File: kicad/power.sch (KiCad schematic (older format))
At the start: 18 parts

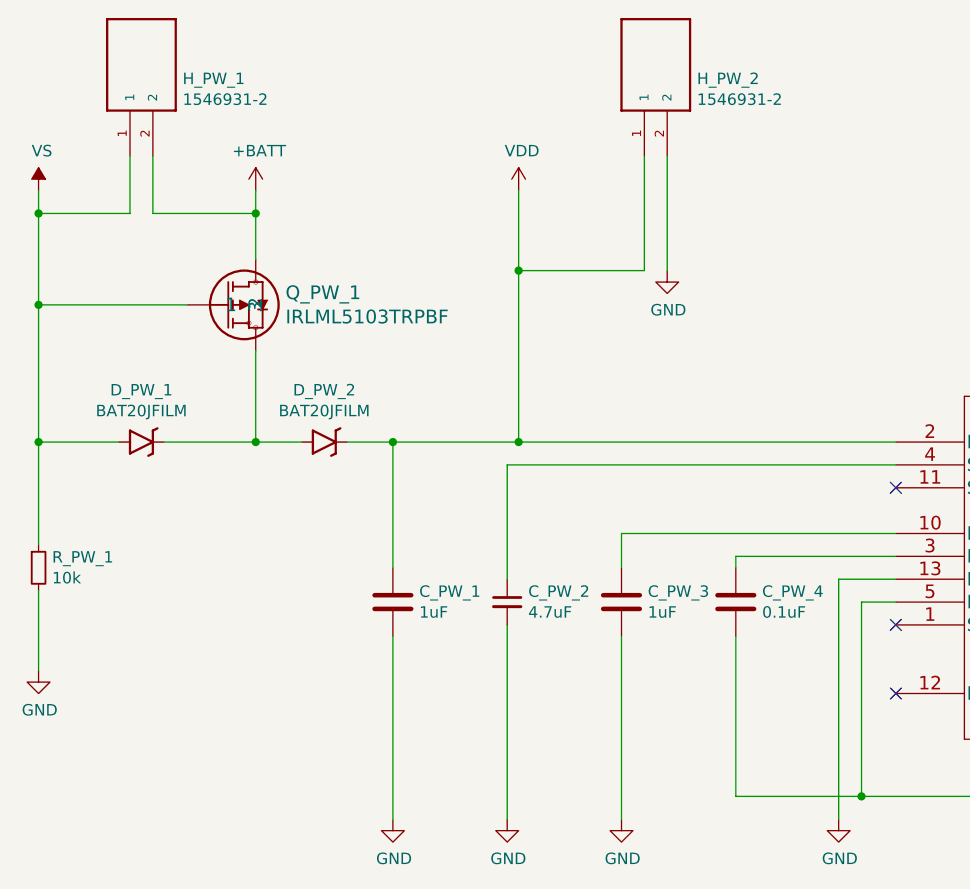
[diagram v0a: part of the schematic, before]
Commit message: Deleted a header pin. Started working on PCB
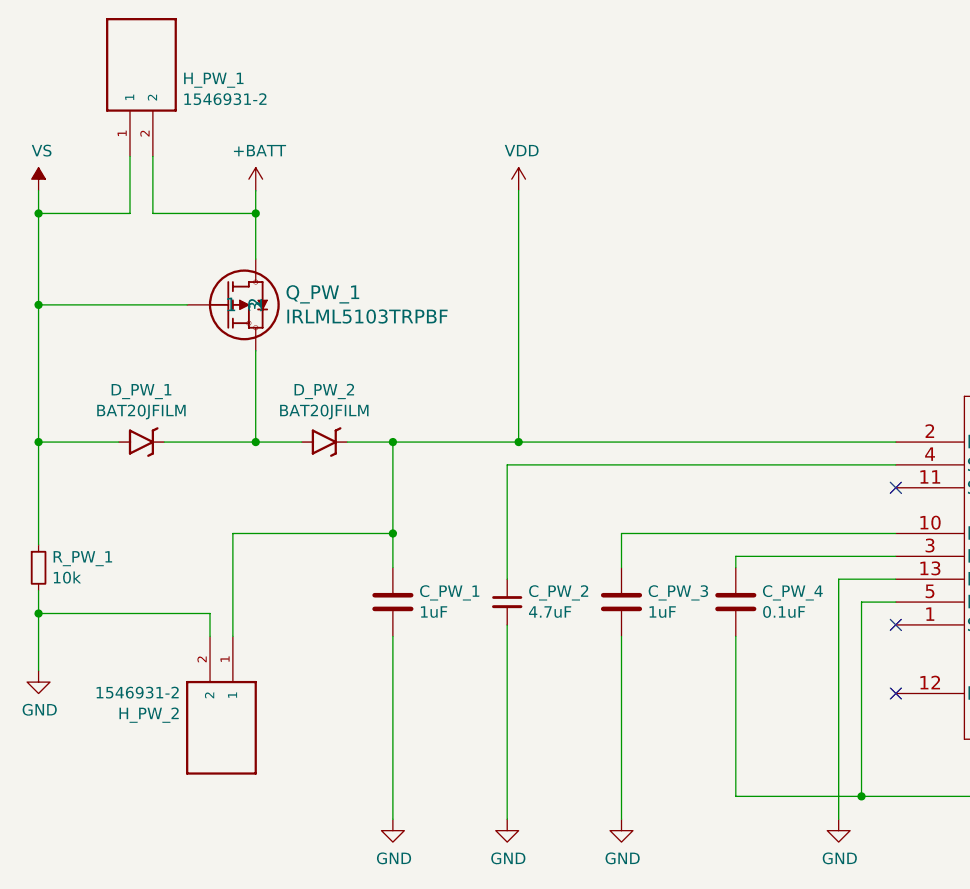
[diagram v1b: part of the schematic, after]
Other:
- moved on the sheet: H_PW_2
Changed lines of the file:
@@
 $Descr A4 11693 8268
 encoding utf-8
-Sheet 2 6
+Sheet 2 5
 Title "ESP32 Sensor Module | Power Supply"
 Date "2020-11-23"
@@
 $EndComp
 $Comp
-L power:+BATT #PWR?
+L power:+BATT #PWR0101
 U 1 1 5FB6F3E3
 P 1850 2200
-F 0 "#PWR?" H 1850 2050 50  0001 C CNN
+F 0 "#PWR0101" H 1850 2050 50  0001 C CNN
 F 1 "+BATT" H 1865 2373 50  0000 C CNN
 F 2 "" H 1850 2200 50  0001 C CNN
@@
 $EndComp
 $Comp
-L power:GND #PWR?
+L power:GND #PWR0102
 U 1 1 5FB9CCF4
 P 3450 4950
-F 0 "#PWR?" H 3450 4700 50  0001 C CNN
+F 0 "#PWR0102" H 3450 4700 50  0001 C CNN
 F 1 "GND" H 3455 4777 50  0000 C CNN
 F 2 "" H 3450 4950 50  0001 C CNN
@@
 $EndComp
 $Comp
-L power:GND #PWR?
+L power:GND #PWR0103
 U 1 1 5FB9D2E5
 P 2950 4950
-F 0 "#PWR?" H 2950 4700 50  0001 C CNN
+F 0 "#PWR0103" H 2950 4700 50  0001 C CNN
 F 1 "GND" H 2955 4777 50  0000 C CNN
 F 2 "" H 2950 4950 50  0001 C CNN
@@
 $EndComp
 $Comp
-L power:GND #PWR?
+L power:GND #PWR0104
 U 1 1 5FC8EA7A
 P 2450 4950
-F 0 "#PWR?" H 2450 4700 50  0001 C CNN
+F 0 "#PWR0104" H 2450 4700 50  0001 C CNN
 F 1 "GND" H 2455 4777 50  0000 C CNN
 F 2 "" H 2450 4950 50  0001 C CNN
@@
 	2450 4150 2450 4950
 $Comp
-L power:VDD #PWR?
+L power:VDD #PWR0105
 U 1 1 5FC9DE63
 P 3000 2200
-F 0 "#PWR?" H 3000 2050 50  0001 C CNN
+F 0 "#PWR0105" H 3000 2050 50  0001 C CNN
 F 1 "VDD" H 3015 2373 50  0000 C CNN
 F 2 "" H 3000 2200 50  0001 C CNN
@@
 $EndComp
 $Comp
-L power:GND #PWR?
+L power:GND #PWR0106
 U 1 1 5FCA653B
 P 900 4300
-F 0 "#PWR?" H 900 4050 50  0001 C CNN
+F 0 "#PWR0106" H 900 4050 50  0001 C CNN
 F 1 "GND" H 905 4127 50  0000 C CNN
 F 2 "" H 900 4300 50  0001 C CNN
@@
 $EndComp
 Wire Wire Line
-	900  4300 900  3950
+	900  4300 900  4050
 Wire Wire Line
 	900  3750 900  3300
@@
 $EndComp
 $Comp
-L power:+3.3V #PWR?
+L power:+3.3V #PWR0107
 U 1 1 5FBC3E26
 P 9200 2800
-F 0 "#PWR?" H 9200 2650 50  0001 C CNN
+F 0 "#PWR0107" H 9200 2650 50  0001 C CNN
 F 1 "+3.3V" H 9215 2973 50  0000 C CNN
 F 2 "" H 9200 2800 50  0001 C CNN
@@
 	9200 4950 9200 4150
 $Comp
-L power:GND #PWR?
+L power:GND #PWR0108
 U 1 1 5FBC26F8
 P 9200 4950
-F 0 "#PWR?" H 9200 4700 50  0001 C CNN
+F 0 "#PWR0108" H 9200 4700 50  0001 C CNN
 F 1 "GND" H 9205 4777 50  0000 C CNN
 F 2 "" H 9200 4950 50  0001 C CNN
@@
 	7250 4950 7250 4500
 $Comp
-L power:GND #PWR?
+L power:GND #PWR0109
 U 1 1 5FBBD9E3
 P 7250 4950
-F 0 "#PWR?" H 7250 4700 50  0001 C CNN
+F 0 "#PWR0109" H 7250 4700 50  0001 C CNN
 F 1 "GND" H 7255 4777 50  0000 C CNN
 F 2 "" H 7250 4950 50  0001 C CNN
@@
 	4650 3900 4400 3900
 $Comp
-L power:GND #PWR?
+L power:GND #PWR0110
 U 1 1 5FB9D73C
 P 4400 4950
-F 0 "#PWR?" H 4400 4700 50  0001 C CNN
+F 0 "#PWR0110" H 4400 4700 50  0001 C CNN
 F 1 "GND" H 4405 4777 50  0000 C CNN
 F 2 "" H 4400 4950 50  0001 C CNN
@@
 	6250 3900 6500 3900
 $Comp
-L power:GND #PWR?
+L power:GND #PWR0111
 U 1 1 5FB7470B
 P 6500 4000
-F 0 "#PWR?" H 6500 3750 50  0001 C CNN
+F 0 "#PWR0111" H 6500 3750 50  0001 C CNN
 F 1 "GND" H 6505 3827 50  0000 C CNN
 F 2 "" H 6500 4000 50  0001 C CNN
@@
 	2250 3300 2450 3300
 Wire Wire Line
-	2450 3850 2450 3300
+	2450 3850 2450 3700
 Connection ~ 2450 3300
 Wire Wire Line
 	2450 3300 3000 3300
 $Comp
-L power:VS #PWR?
+L power:VS #PWR0112
 U 1 1 5FDE6D6A
 P 900 2200
-F 0 "#PWR?" H 700 2050 50  0001 C CNN
+F 0 "#PWR0112" H 700 2050 50  0001 C CNN
 F 1 "VS" H 915 2373 50  0000 C CNN
 F 2 "" H 900 2200 50  0001 C CNN
@@
 L 1546931-2:1546931-2 H_PW_2
 U 1 1 5FDE97E8
-P 3650 1650
-F 0 "H_PW_2" V 3589 1520 50  0000 R CNN
-F 1 "1546931-2" V 3498 1520 50  0000 R CNN
-F 2 "footprints:1546931-2" H 3650 1650 50  0001 L BNN
-F 3 "https://www.te.com/commerce/DocumentDelivery/DDEController?Action=srchrtrv&DocNm=1-1773458-1_EURO_STYLE_QRG&DocType=DS&DocLang=English" H 3650 1650 50  0001 L BNN
-F 4 "1546931-2" H 3650 1650 50  0001 C CNN "Part Name"
-F 5 "TE Connectivity AMP Connectors" H 3650 1650 50  0001 C CNN "Manufacturer"
-F 6 "Digikey Canada" H 3650 1650 50  0001 C CNN "Vendor"
-F 7 "" H 3650 1650 50  0001 C CNN "digikeypn"
-F 8 "" H 3650 1650 50  0001 C CNN "Vendor Part Number"
-F 9 "A97965-ND" H 3650 1650 50  0001 C CNN "Vendor Part Name"
-	1    3650 1650
-	0    -1   -1   0
-$EndComp
-Wire Wire Line
-	3000 2200 3000 2550
-Wire Wire Line
-	3550 2050 3550 2550
-Wire Wire Line
-	3550 2550 3000 2550
-Connection ~ 3000 2550
-Wire Wire Line
-	3000 2550 3000 3300
-$Comp
-L power:GND #PWR?
-U 1 1 5FDF0ABA
-P 3650 2550
-F 0 "#PWR?" H 3650 2300 50  0001 C CNN
-F 1 "GND" H 3655 2377 50  0000 C CNN
-F 2 "" H 3650 2550 50  0001 C CNN
-F 3 "" H 3650 2550 50  0001 C CNN
-	1    3650 2550
-	1    0    0    -1
-$EndComp
-Wire Wire Line
-	3650 2550 3650 2050
+P 1650 4550
+F 0 "H_PW_2" V 1589 4420 50  0000 R CNN
+F 1 "1546931-2" V 1498 4420 50  0000 R CNN
+F 2 "footprints:1546931-2" H 1650 4550 50  0001 L BNN
+F 3 "https://www.te.com/commerce/DocumentDelivery/DDEController?Action=srchrtrv&DocNm=1-1773458-1_EURO_STYLE_QRG&DocType=DS&DocLang=English" H 1650 4550 50  0001 L BNN
+F 4 "1546931-2" H 1650 4550 50  0001 C CNN "Part Name"
+F 5 "TE Connectivity AMP Connectors" H 1650 4550 50  0001 C CNN "Manufacturer"
+F 6 "Digikey Canada" H 1650 4550 50  0001 C CNN "Vendor"
+F 7 "" H 1650 4550 50  0001 C CNN "digikeypn"
+F 8 "" H 1650 4550 50  0001 C CNN "Vendor Part Number"
+F 9 "A97965-ND" H 1650 4550 50  0001 C CNN "Vendor Part Name"
+	1    1650 4550
+	0    1    1    0
+$EndComp
+Wire Wire Line
+	3000 2200 3000 3300
+Wire Wire Line
+	1650 4150 1650 4050
+Wire Wire Line
+	1650 4050 900  4050
+Connection ~ 900  4050
+Wire Wire Line
+	900  4050 900  3950
+Wire Wire Line
+	1750 4150 1750 3700
+Wire Wire Line
+	1750 3700 2450 3700
+Connection ~ 2450 3700
+Wire Wire Line
+	2450 3700 2450 3300
 $EndSCHEMATC

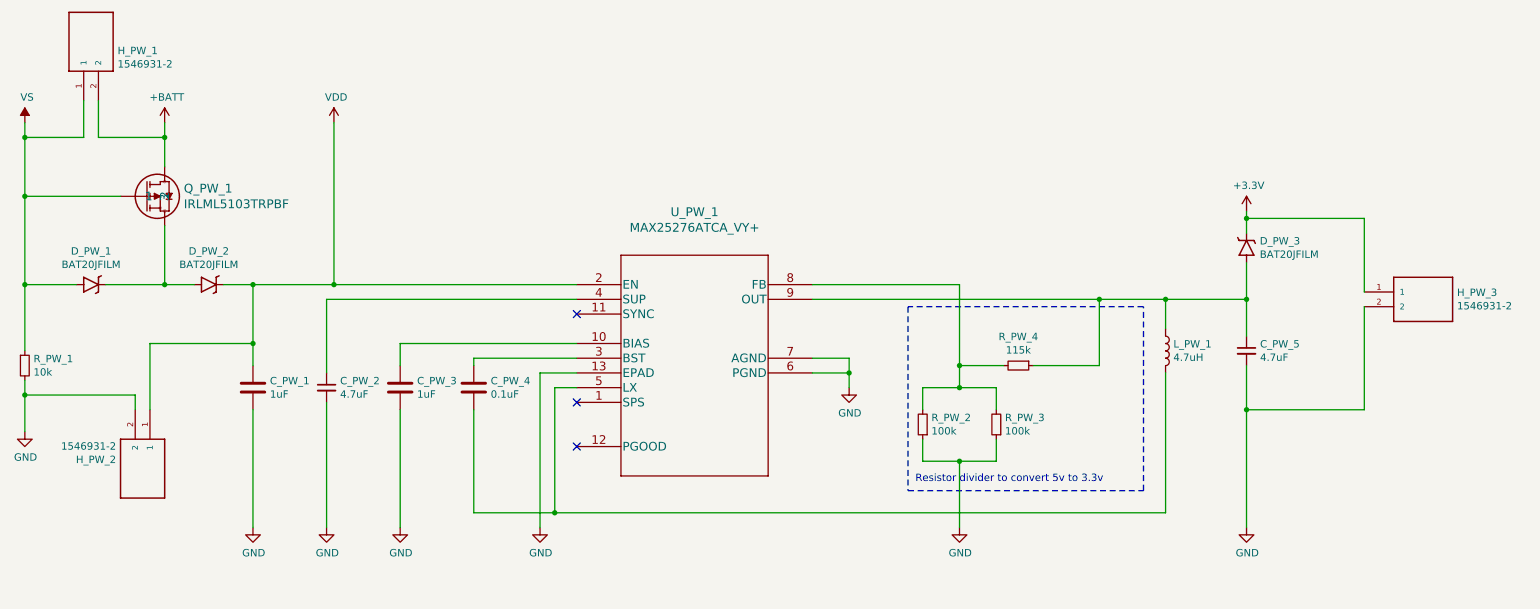
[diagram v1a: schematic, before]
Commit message: Updated schematic and PCB design to v0.0.2 for 2-layer pcb. Added more silkscreen text
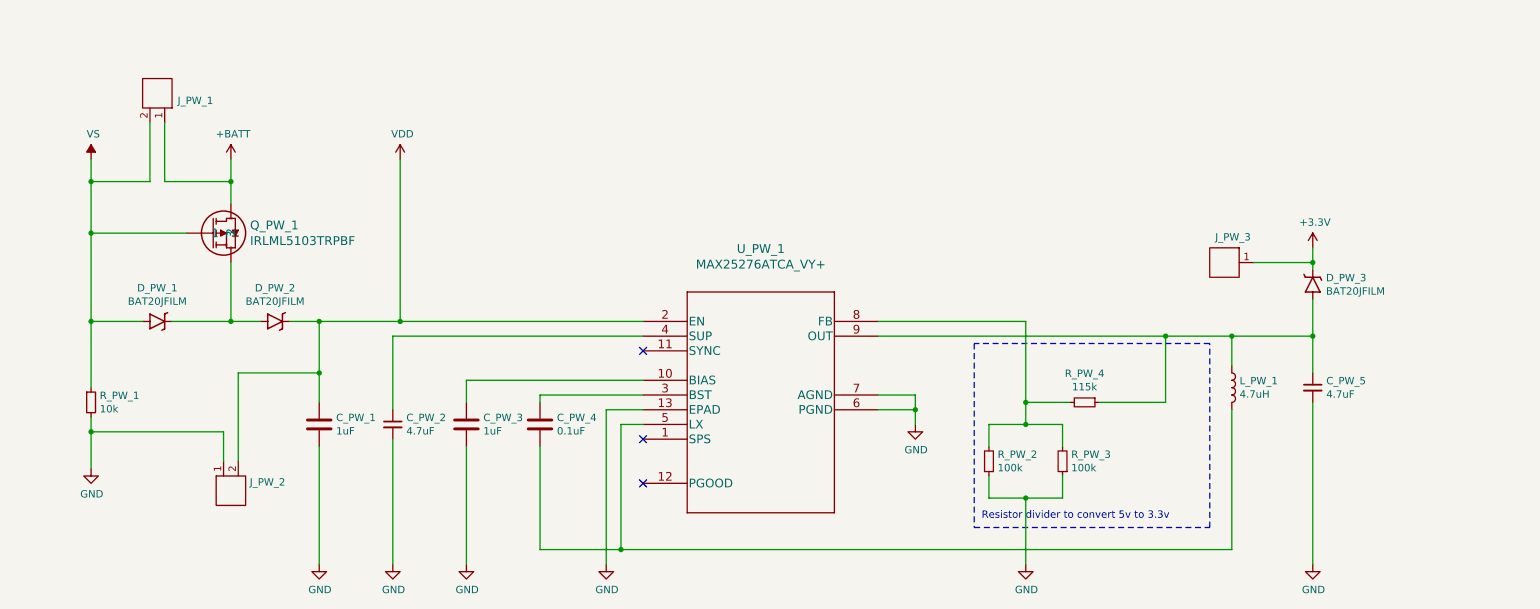
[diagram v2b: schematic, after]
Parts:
- removed H_PW_1, H_PW_2, H_PW_3: 1546931-2, footprints:1546931-2, symbol 1546931-2:1546931-2
- added J_PW_1, J_PW_2: Header_Pin_2, Connector_PinHeader_2.54mm:PinHeader_1x02_P2.54mm_Vertical, symbol CANtech:Header_Pin_2
- added J_PW_3: Header_Pin_1, Connector_PinHeader_2.54mm:PinHeader_1x01_P2.54mm_Vertical, symbol CANtech:Header_Pin_1
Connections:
- net +3V3: now also J_PW_3.1
- net +BATT: now also J_PW_1.1
- net GND: now also J_PW_2.1
- net VDD: now also J_PW_2.2
- net VS: now also J_PW_1.2
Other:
- moved on the sheet: C_PW_1, C_PW_2, C_PW_3, C_PW_4, C_PW_5, D_PW_1, D_PW_2, D_PW_3, L_PW_1, Q_PW_1, R_PW_1, R_PW_2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
